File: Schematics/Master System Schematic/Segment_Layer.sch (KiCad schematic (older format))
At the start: 0 parts

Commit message: Segment Layer
> Added segments to Segment_Layer sheet
> Added VT PCBs and Thermistor PCBs to Segment_Layer sheet
> Removed relays from VT PCBs
> Still need to add connectors to VT and Thermistor PCBs once PCBs have been redesigned
> Added outputs for Segment_Layer sheet
> Added wire gauges to Segment_Layer sheet

Segment_Layer V1.0
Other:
- note added: "2AWG\n"
- note added: "44x 22AWG"

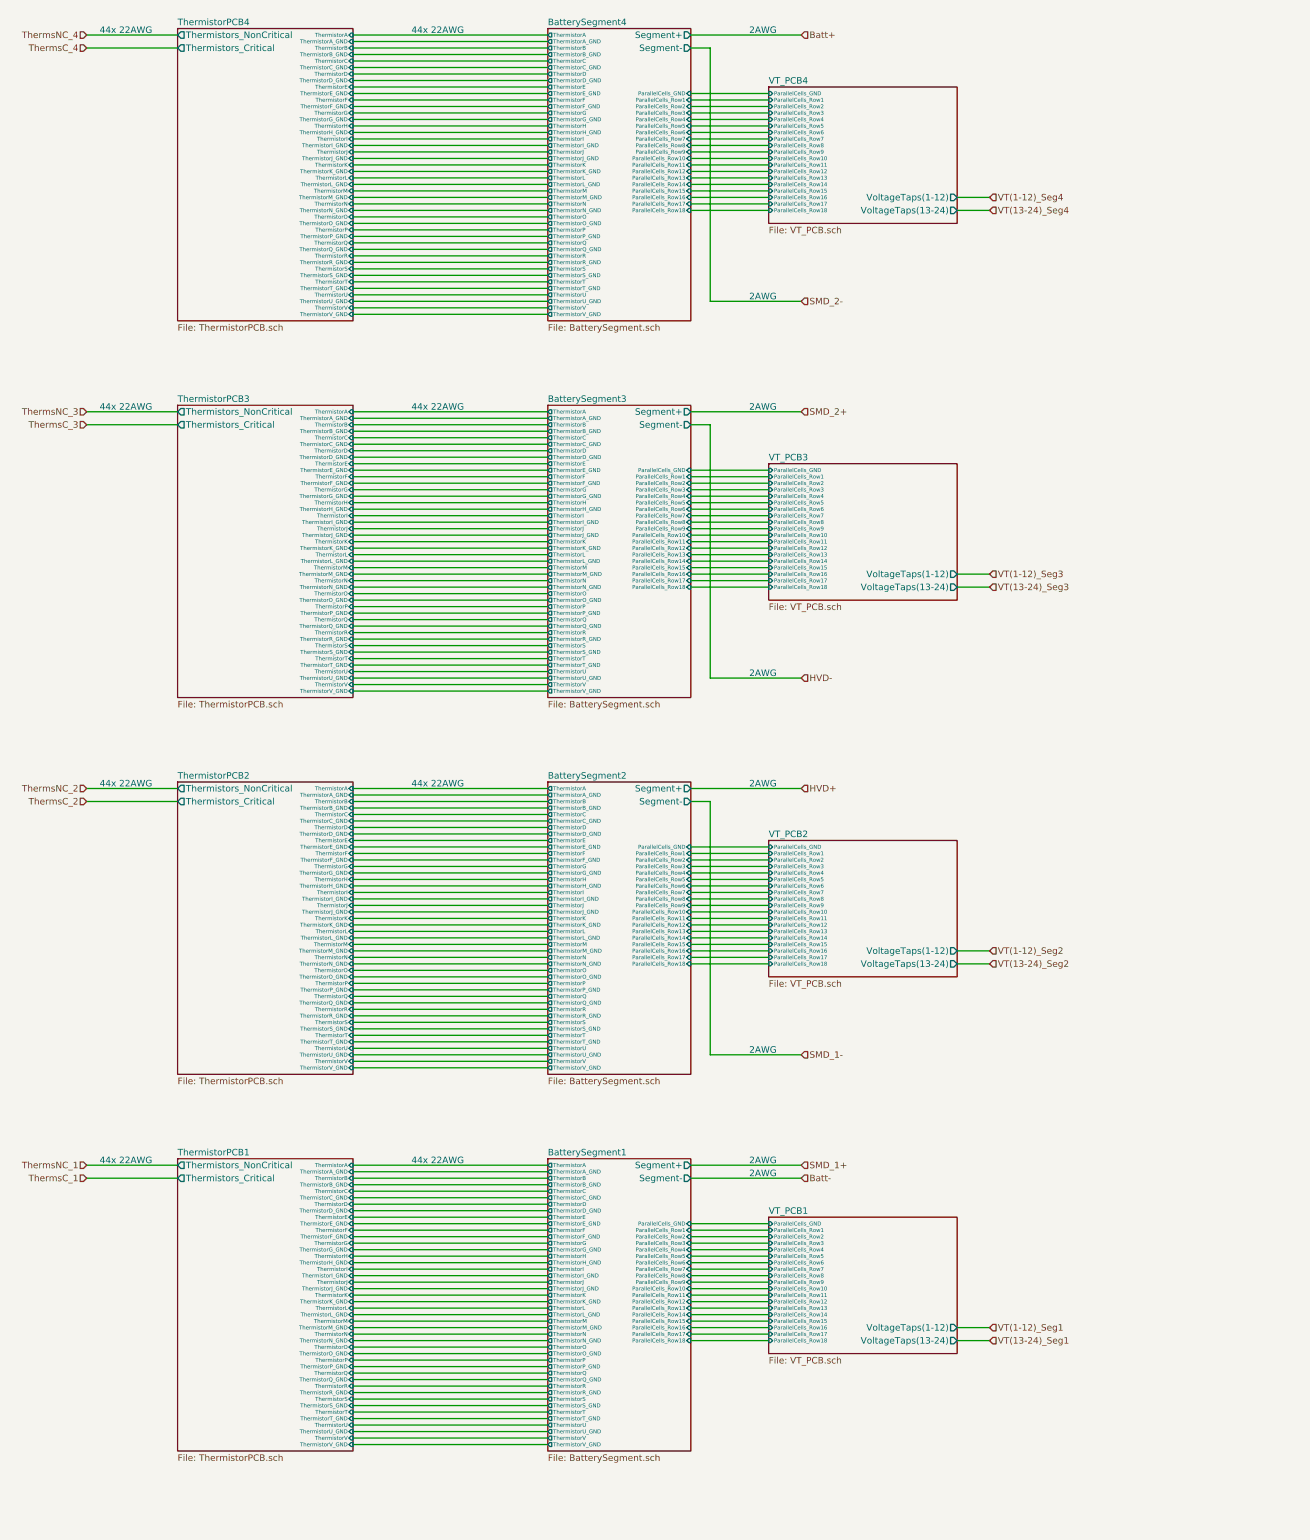
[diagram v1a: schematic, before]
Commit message: LV Plate
> Added basic connectors and outlines for MCR PCB
> Added and wired components on LV Plate
> Added GLV connector
> Connected layers
> Some wire gauges still needed

LV_Plate Version 1.0
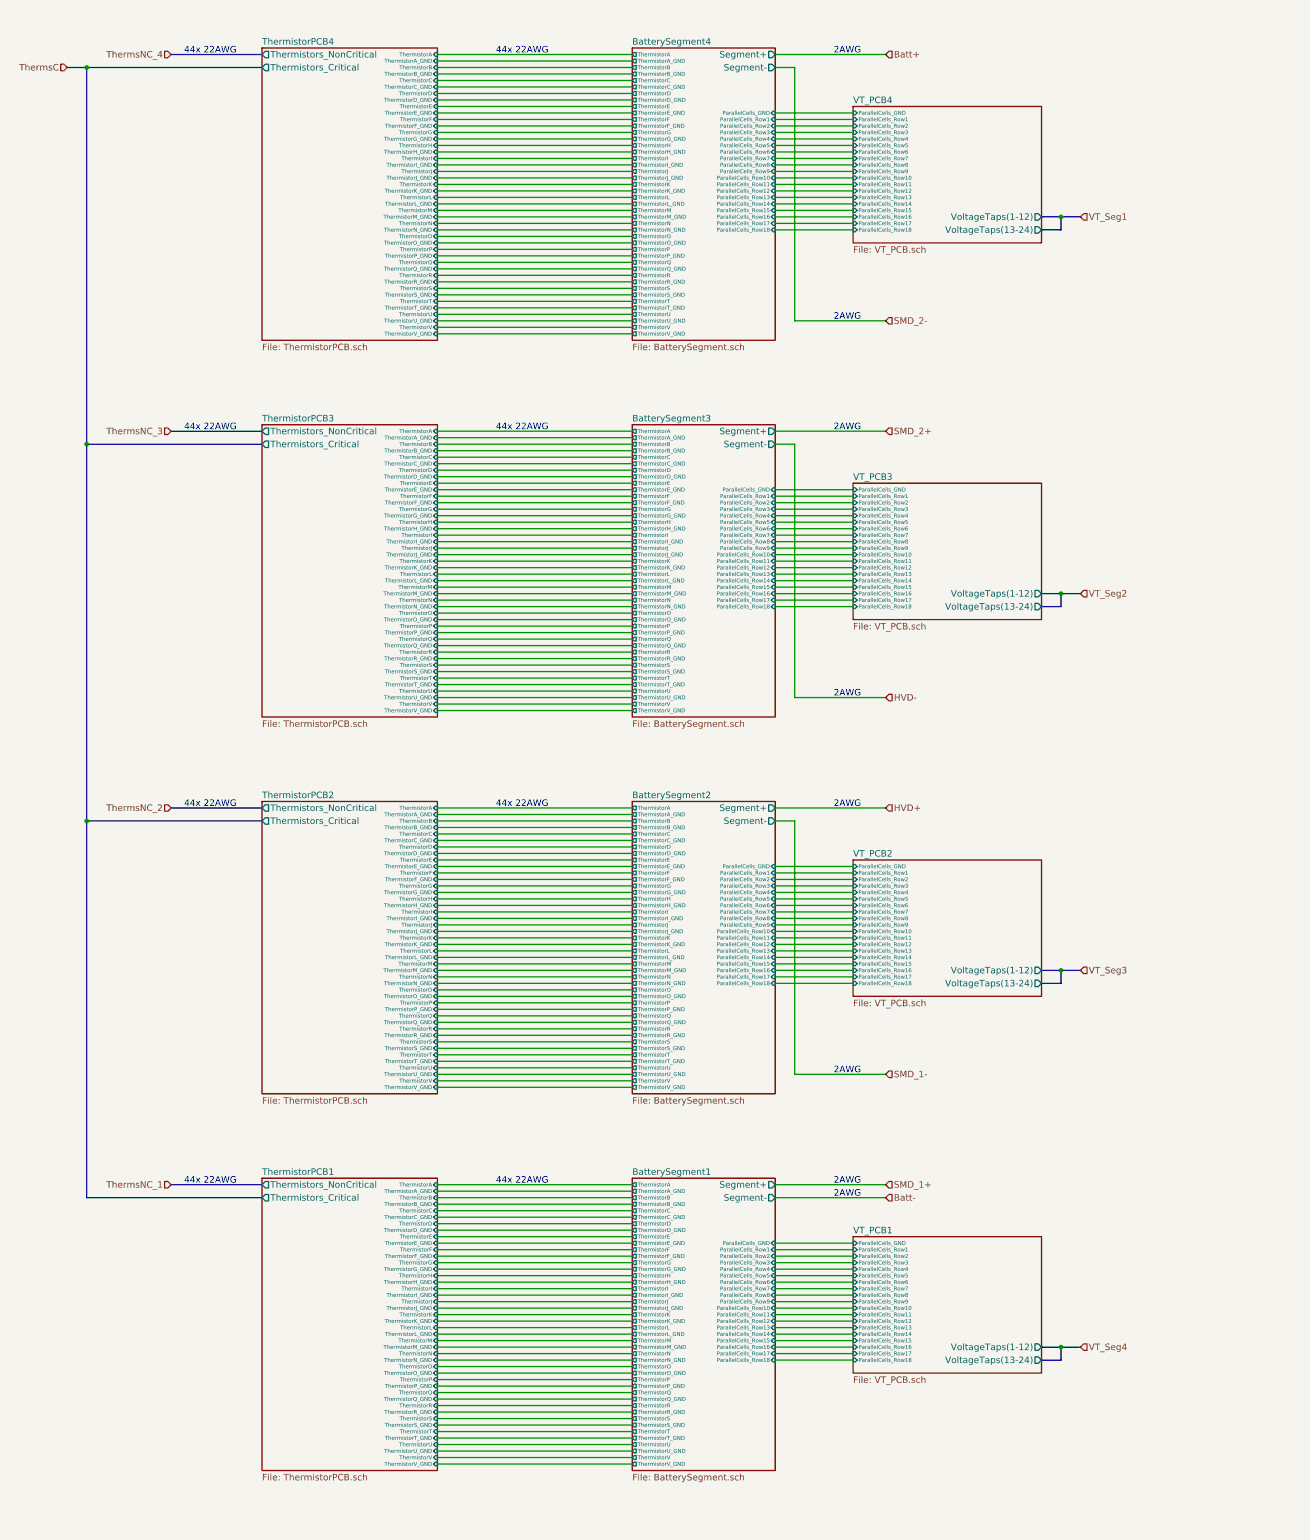
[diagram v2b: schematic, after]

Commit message: LV Plate Cleanup + Other Small Stuff
> Renamed MCR PCB to BattBox PCB
> Added 7 Pin IMD connector to BattBox PCB
> Fixed wire gauges on Segment Layer sheet
> Added HV cutout on LV Plate
> Added fan signals
> Deleted old accumulator stuff
> Added BattBox and BMS fans

BattBox PCB V1.0
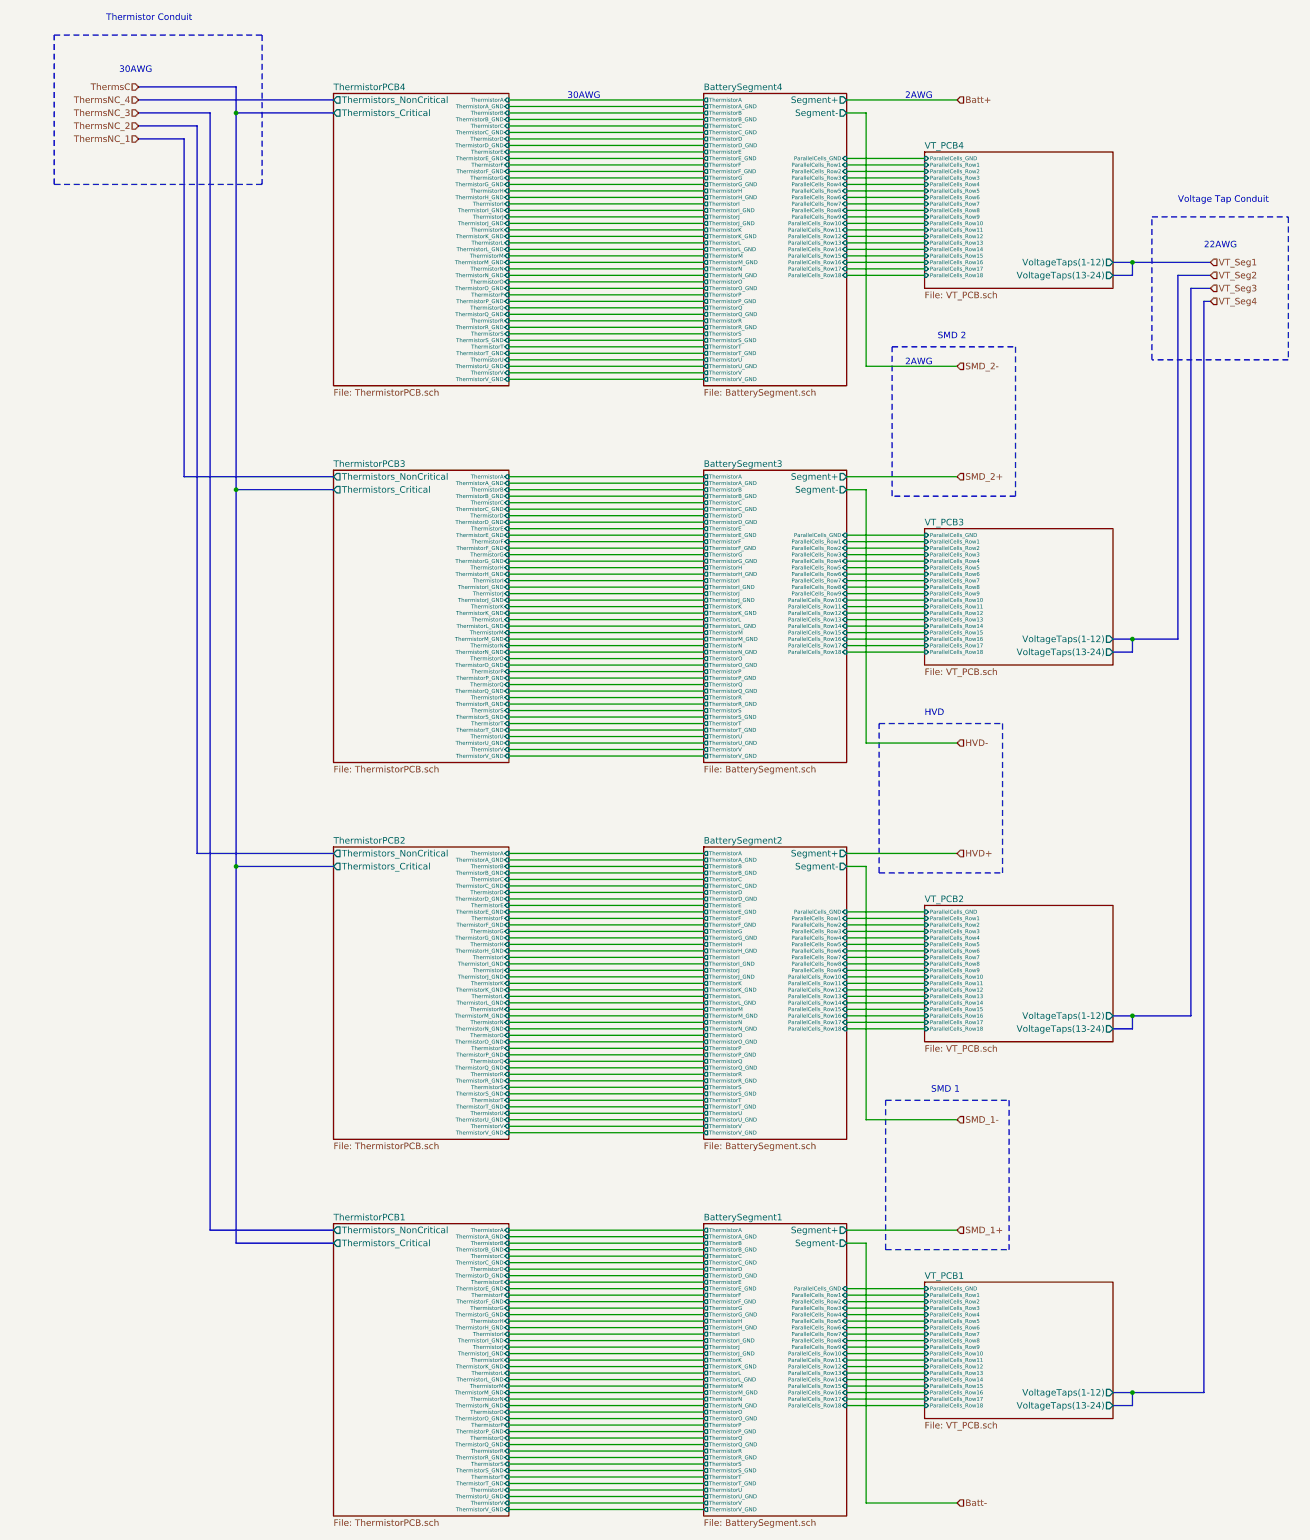
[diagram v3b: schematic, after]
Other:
- note added: "22AWG"
- note added: "30AWG"
- note added: "HVD"
- note added: "SMD 1"
- note added: "SMD 2"
- note added: "Thermistor Conduit"
- note added: "Voltage Tap Conduit"
- note removed: "44x 22AWG"
